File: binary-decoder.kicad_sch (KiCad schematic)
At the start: 2 parts, among them U11 74AUC2G04, U12 74LS08

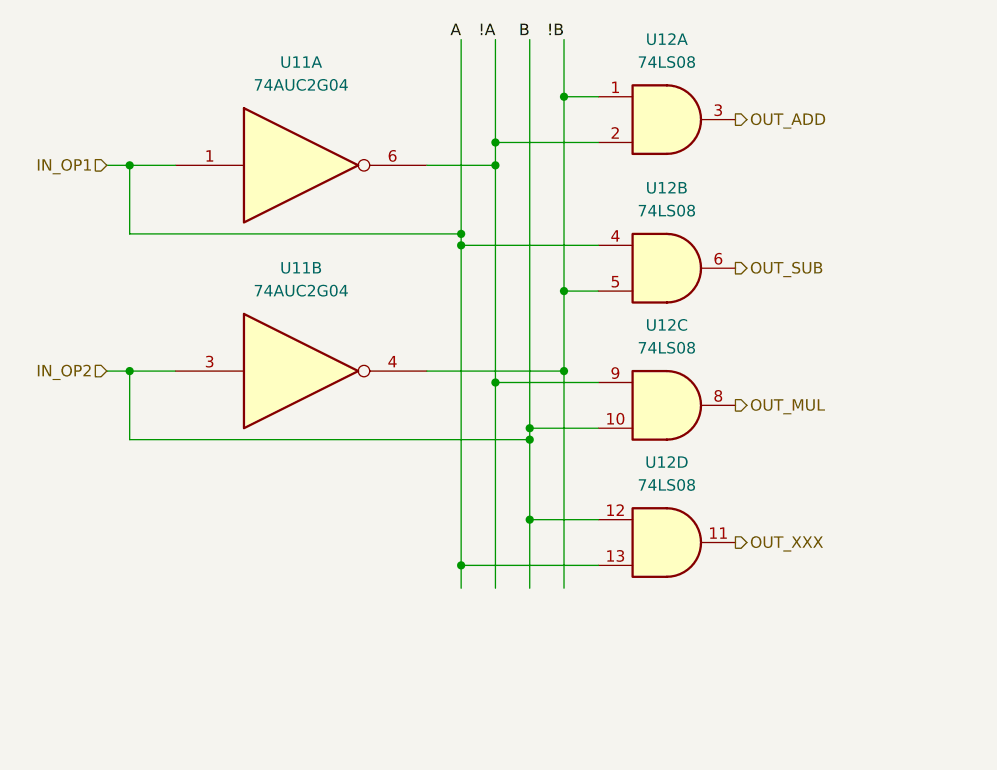
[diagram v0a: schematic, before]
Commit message: feat: removed ERC errors
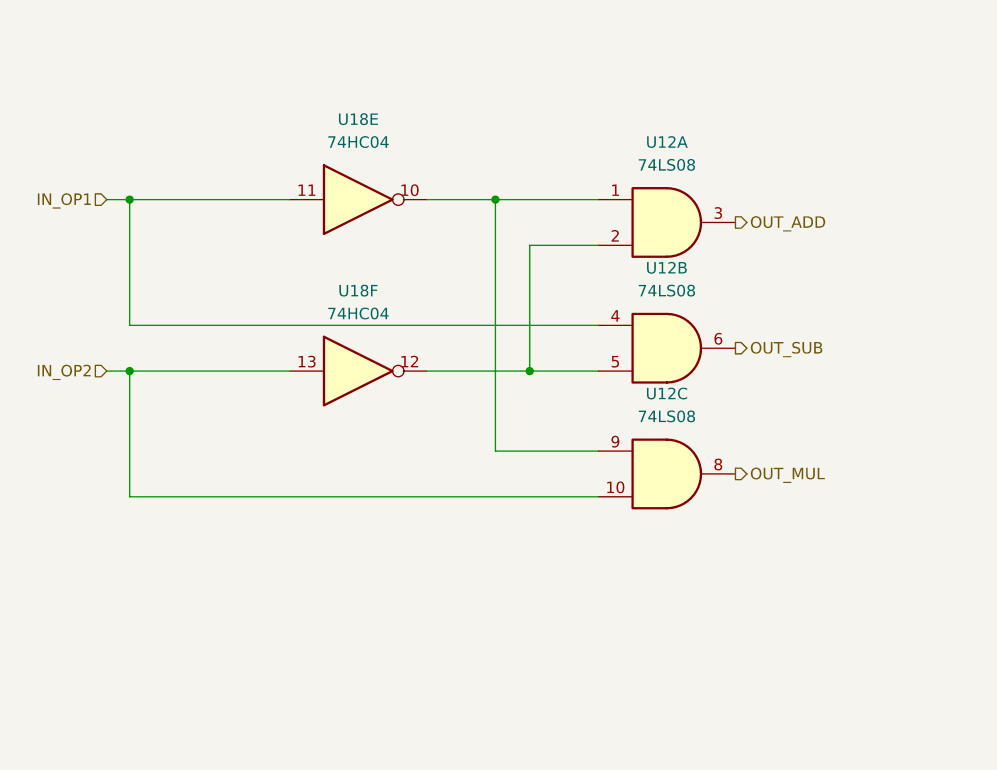
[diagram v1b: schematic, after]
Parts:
- removed U11: 74AUC2G04, symbol 74xGxx:74AUC2G04
- removed unit 4 of U12
- added U18: 74HC04, symbol 74xx:74HC04
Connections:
- net IN_OP1: now also U18.11
- net IN_OP2: now also U18.13
- net !A: no longer names the net of U12.2
- net !A: now also U12.5, U18.12; no longer U12.9
- net !B: no longer names the net of U12.1
- net !B: now also U12.9, U18.10; no longer U12.5
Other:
- moved on the sheet: U12A, U12B, U12C

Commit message: fix: removed ERC warnings and errors
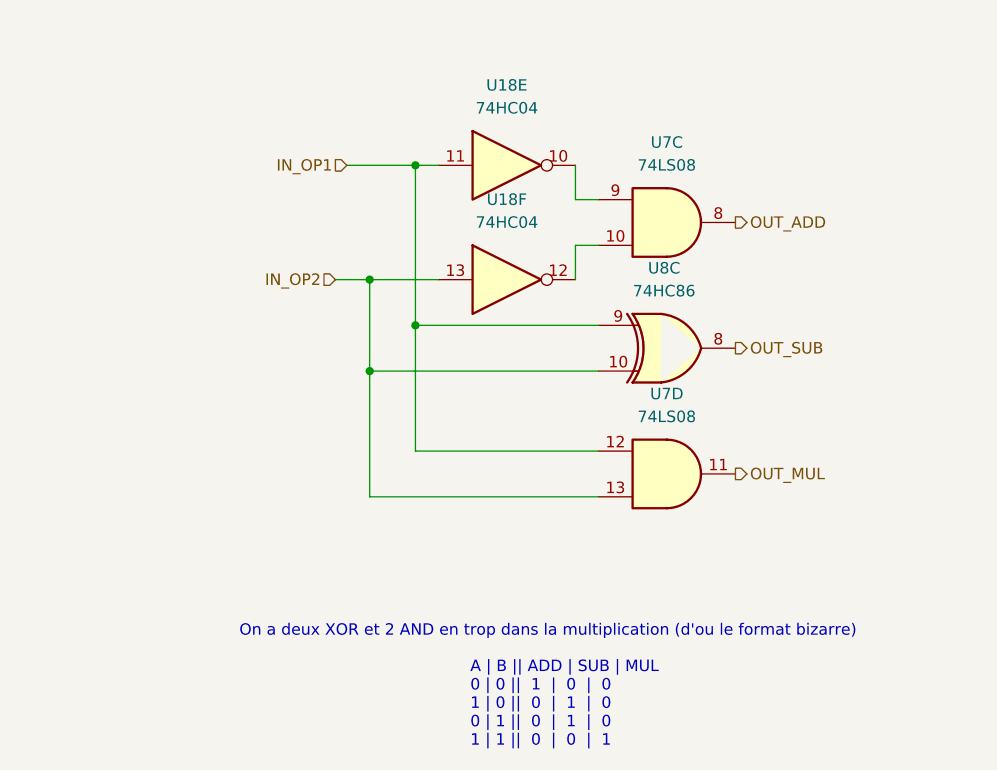
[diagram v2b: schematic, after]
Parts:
- removed unit 2 of U12
- added U8: 74HC86, symbol 74xx:74HC86
- renumbered U12 to U7
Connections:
- net IN_OP1: now also U7.12, U8.9
- net IN_OP2: now also U7.13, U8.10; no longer U7.10
- net OUT_ADD: now also U7.8; no longer U7.3
- net OUT_MUL: now also U7.11; no longer U7.8
- net OUT_SUB: now also U8.8
- net at U18.12: now also U7.10; no longer U7.2
- new net: U18.10, U7.9
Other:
- note added: "A | B || ADD | SUB | MUL 0 | 0 || 1 | 0 | 0 1 | 0 || 0 | 1 | 0 0 | 1 || 0 | 1 | 0 1 | 1 || 0 | 0 | 1"
- note added: "On a deux XOR et 2 AND en trop dans la multiplication (d'ou le format bizarre)"
- moved on the sheet: U18E, U18F

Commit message: feat: NOT to mofset + first batch of footprint
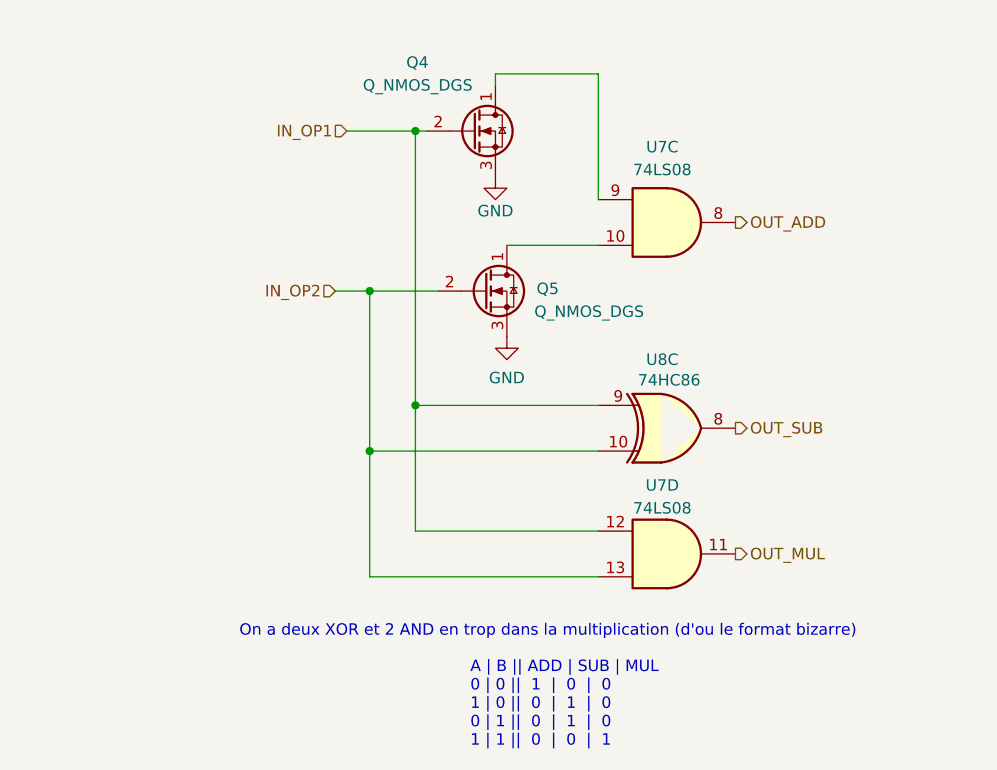
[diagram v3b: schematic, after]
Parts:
- removed U18: 74HC04, symbol 74xx:74HC04
- added Q4, Q5: Q_NMOS_DGS, symbol Transistor_FET:Q_NMOS_DGS
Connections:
- net IN_OP1: now also Q4.2 (G)
- net IN_OP2: now also Q5.2 (G)
- net at U7.10: now also Q5.1 (D)
- net at U7.9: now also Q4.1 (D)
- new net GND: Q4.3 (S), Q5.3 (S)
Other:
- moved on the sheet: U7D, U8C

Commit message: feat: added footprint for mofsets
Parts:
- Q4, Q5: footprint (none) -> Package_TO_SOT_SMD:SOT-23

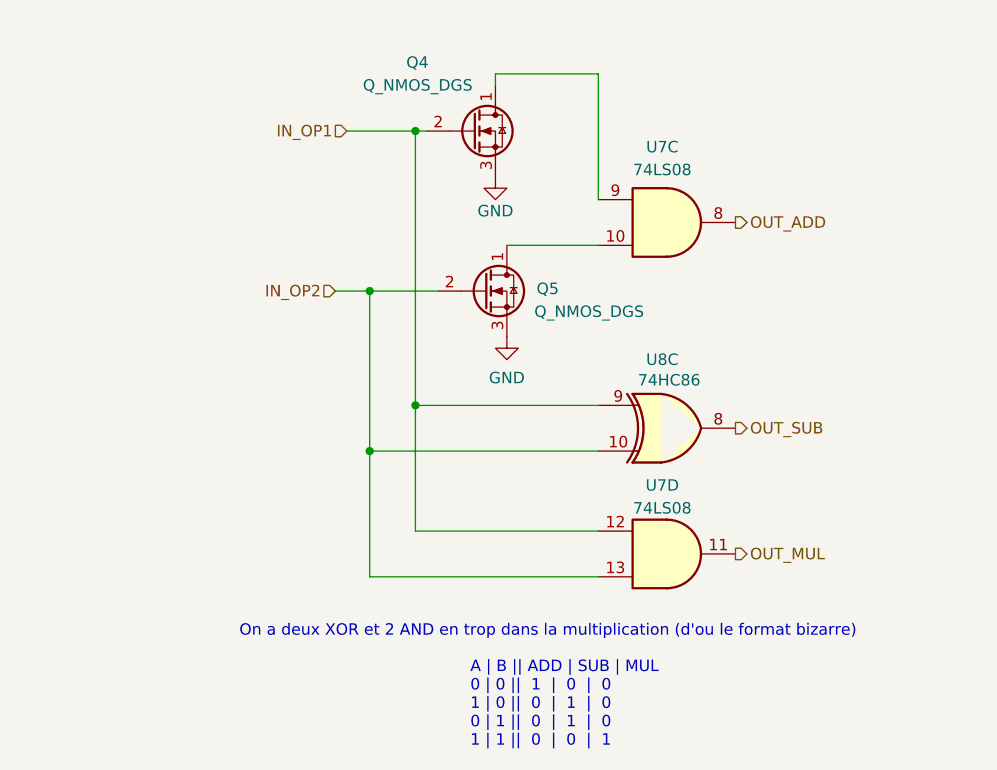
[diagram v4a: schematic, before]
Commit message: feat: footprints on gates
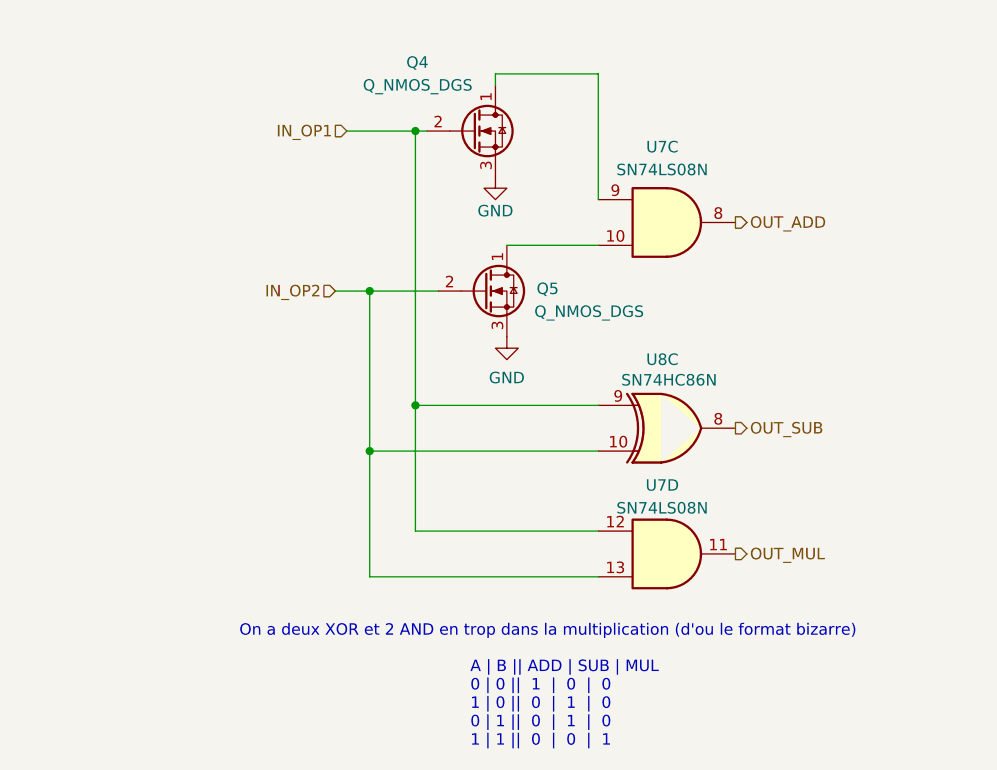
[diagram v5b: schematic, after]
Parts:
- U7: value 74LS08 -> SN74LS08N; footprint (none) -> Package_DIP:DIP-14_W7.62mm_LongPads
- U8: value 74HC86 -> SN74HC86N; footprint (none) -> Package_DIP:DIP-14_W7.62mm_LongPads
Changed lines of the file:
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@@
 			)
 		)
-		(property "Value" "74HC86"
+		(property "Value" "SN74HC86N"
 			(at 147.574 112.776 0)
 			(show_name no)
@@
 			)
 		)
-		(property "Footprint" ""
+		(property "Footprint" "Package_DIP:DIP-14_W7.62mm_LongPads"
 			(at 147.32 118.11 0)
 			(hide yes)
@@
 			)
 		)
-		(property "Value" "74LS08"
+		(property "Value" "SN74LS08N"
 			(at 146.812 127 0)
 			(show_name no)
@@
 			)
 		)
-		(property "Footprint" ""
+		(property "Footprint" "Package_DIP:DIP-14_W7.62mm_LongPads"
 			(at 147.32 132.08 0)
 			(hide yes)
@@
 			)
 		)
-		(property "Datasheet" "http://www.ti.com/lit/gpn/sn74LS08"
+		(property "Datasheet" "https://www.ti.com/lit/ds/symlink/sn74hc86.pdf"
 			(at 147.32 132.08 0)
 			(hide yes)
@@
 			)
 		)
-		(property "Value" "74LS08"
+		(property "Value" "SN74LS08N"
 			(at 146.812 89.408 0)
 			(show_name no)
@@
 			)
 		)
-		(property "Footprint" ""
+		(property "Footprint" "Package_DIP:DIP-14_W7.62mm_LongPads"
 			(at 147.32 95.25 0)
 			(hide yes)
@@
 			)
 		)
-		(property "Datasheet" "http://www.ti.com/lit/gpn/sn74LS08"
+		(property "Datasheet" "https://www.ti.com/lit/ds/symlink/sn74hc86.pdf"
 			(at 147.32 95.25 0)
 			(hide yes)

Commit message: fix: updated footprint for mofset to 23-3 and switch to HandSoldering type
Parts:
- Q4, Q5: footprint Package_TO_SOT_SMD:SOT-23 -> Package_TO_SOT_SMD:SOT-23-3
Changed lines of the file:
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@@
 			)
 		)
-		(property "Footprint" "Package_TO_SOT_SMD:SOT-23"
+		(property "Footprint" "Package_TO_SOT_SMD:SOT-23-3"
 			(at 132.08 100.33 0)
 			(hide yes)
@@
 			)
 		)
-		(property "Footprint" "Package_TO_SOT_SMD:SOT-23"
+		(property "Footprint" "Package_TO_SOT_SMD:SOT-23-3"
 			(at 130.81 82.55 0)
 			(hide yes)

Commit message: fix: merge
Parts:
- renumbered Q4 to Q0, Q5 to Q1, U7 to U6
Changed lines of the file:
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@@
 		(in_pos_files yes)
 		(dnp no)
-		(property "Reference" "Q5"
+		(property "Reference" "Q1"
 			(at 132.842 102.616 0)
 			(show_name no)
@@
 			(project "alu"
 				(path "/4987240f-8890-46b8-b8e9-0d60580cb205/54811f93-c5c3-45f8-b60d-f728802dc286"
-					(reference "Q5")
+					(reference "Q1")
 					(unit 1)
 				)
@@
 		(in_pos_files yes)
 		(dnp no)
-		(property "Reference" "#PWR033"
+		(property "Reference" "#PWR?"
 			(at 129.54 114.3 0)
 			(hide yes)
@@
 			(project "alu"
 				(path "/4987240f-8890-46b8-b8e9-0d60580cb205/54811f93-c5c3-45f8-b60d-f728802dc286"
-					(reference "#PWR033")
+					(reference "#PWR?")
 					(unit 1)
 				)
@@
 		(in_pos_files yes)
 		(dnp no)
-		(property "Reference" "#PWR028"
+		(property "Reference" "#PWR?"
 			(at 128.27 96.52 0)
 			(hide yes)
@@
 			(project "alu"
 				(path "/4987240f-8890-46b8-b8e9-0d60580cb205/54811f93-c5c3-45f8-b60d-f728802dc286"
-					(reference "#PWR028")
+					(reference "#PWR?")
 					(unit 1)
 				)
@@
 		(in_pos_files yes)
 		(dnp no)
-		(property "Reference" "Q4"
+		(property "Reference" "Q0"
 			(at 118.364 77.47 0)
 			(show_name no)
@@
 			(project "alu"
 				(path "/4987240f-8890-46b8-b8e9-0d60580cb205/54811f93-c5c3-45f8-b60d-f728802dc286"
-					(reference "Q4")
+					(reference "Q0")
 					(unit 1)
 				)
@@
 		(in_pos_files yes)
 		(dnp no)
-		(property "Reference" "U7"
+		(property "Reference" "U6"
 			(at 146.812 124.46 0)
 			(show_name no)
@@
 			(project "alu"
 				(path "/4987240f-8890-46b8-b8e9-0d60580cb205/54811f93-c5c3-45f8-b60d-f728802dc286"
-					(reference "U7")
+					(reference "U6")
 					(unit 4)
 				)
@@
 		(in_pos_files yes)
 		(dnp no)
-		(property "Reference" "U7"
+		(property "Reference" "U6"
 			(at 146.812 86.868 0)
 			(show_name no)
@@
 			(project "alu"
 				(path "/4987240f-8890-46b8-b8e9-0d60580cb205/54811f93-c5c3-45f8-b60d-f728802dc286"
-					(reference "U7")
+					(reference "U6")
 					(unit 3)
 				)
